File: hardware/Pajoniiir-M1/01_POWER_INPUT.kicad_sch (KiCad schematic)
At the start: 17 parts, among them J1 5V_LOCKING_INPUT_TBD, U7 TPS259474ARPWR

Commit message: hardware: declare verified rail power sources for ERC
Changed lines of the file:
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@@
     (effects (font (size 1.27 1.27)))
+  )
+  (symbol
+    (lib_id "power:PWR_FLAG")
+    (at 120.015 50.165 0)
+    (unit 1)
+    (exclude_from_sim no)
+    (in_bom yes)
+    (on_board yes)
+    (dnp no)
+    (property "Reference" "#FLG0101" (at 120.015 52.07 0) (effects (font (size 1.27 1.27)) (hide yes)))
+    (property "Value" "PWR_FLAG" (at 120.015 53.975 0) (effects (font (size 1.27 1.27))))
+    (property "Footprint" "" (at 120.015 50.165 0) (effects (font (size 1.27 1.27)) (hide yes)))
+    (property "Datasheet" "~" (at 120.015 50.165 0) (effects (font (size 1.27 1.27)) (hide yes)))
+    (property "Description" "Special symbol for telling ERC where power comes from" (at 120.015 50.165 0) (effects (font (size 1.27 1.27)) (hide yes)))
+    (pin "1")
+    (instances (project "Pajoniiir-M1" (path "/2c8dd352-b7b8-4d9e-8f93-5dd43be2a100/31000001-6b2a-4a3a-8c91-000000000001" (reference "#FLG0101") (unit 1))))
+  )
+  (symbol
+    (lib_id "power:PWR_FLAG")
+    (at 19.685 47.625 0)
+    (unit 1)
+    (exclude_from_sim no)
+    (in_bom yes)
+    (on_board yes)
+    (dnp no)
+    (property "Reference" "#FLG0102" (at 19.685 49.53 0) (effects (font (size 1.27 1.27)) (hide yes)))
+    (property "Value" "PWR_FLAG" (at 19.685 51.435 0) (effects (font (size 1.27 1.27))))
+    (property "Footprint" "" (at 19.685 47.625 0) (effects (font (size 1.27 1.27)) (hide yes)))
+    (property "Datasheet" "~" (at 19.685 47.625 0) (effects (font (size 1.27 1.27)) (hide yes)))
+    (property "Description" "Special symbol for telling ERC where power comes from" (at 19.685 47.625 0) (effects (font (size 1.27 1.27)) (hide yes)))
+    (pin "1")
+    (instances (project "Pajoniiir-M1" (path "/2c8dd352-b7b8-4d9e-8f93-5dd43be2a100/31000001-6b2a-4a3a-8c91-000000000001" (reference "#FLG0102") (unit 1))))
   )
   (sheet_instances

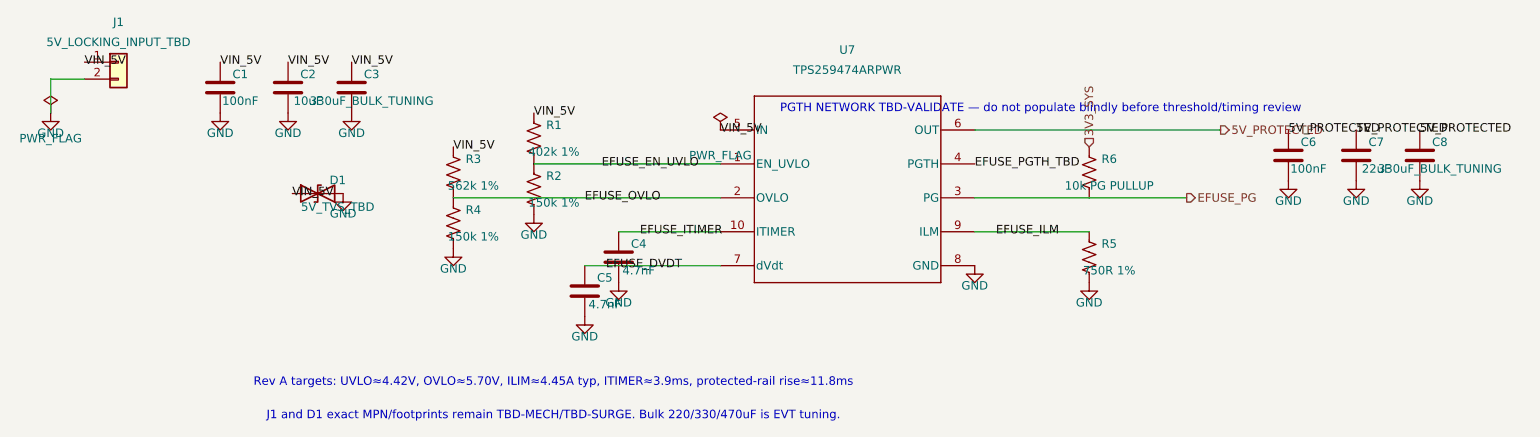
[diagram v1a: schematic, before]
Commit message: hardware: lock TPS259474 PGTH at 4.49V
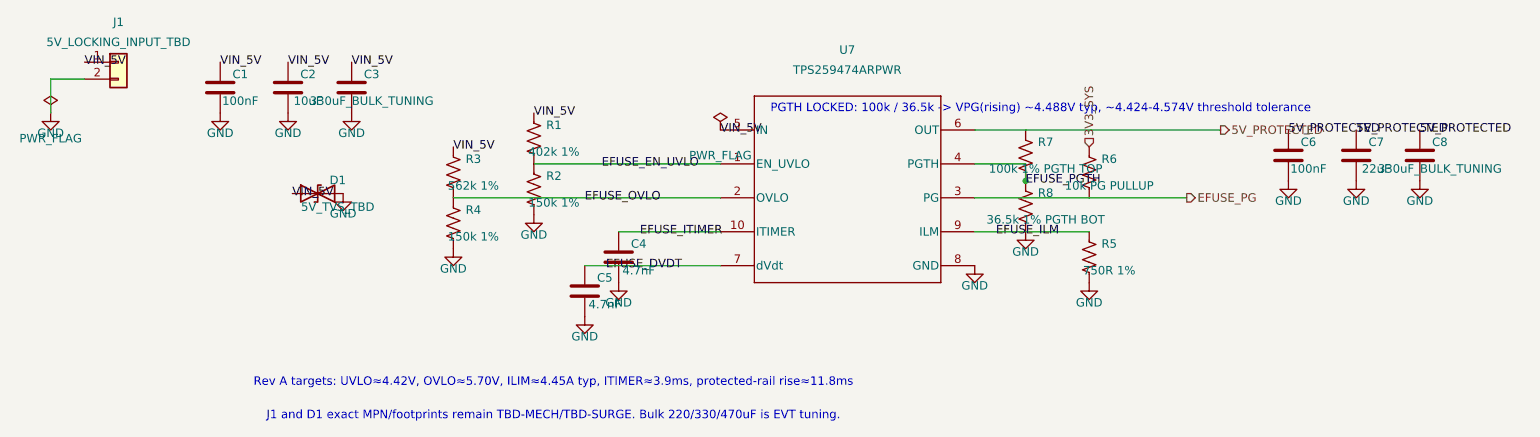
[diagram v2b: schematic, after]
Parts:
- added R7: 100k 1% PGTH TOP, Resistor_SMD:R_0603_1608Metric, symbol Device:R_US
- added R8: 36.5k 1% PGTH BOT, Resistor_SMD:R_0603_1608Metric, symbol Device:R_US
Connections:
- net GND: now also R8.2
- net EFUSE_PGTH_TBD renamed EFUSE_PGTH
- net EFUSE_PGTH: now also R7.2, R8.1
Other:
- note added: "PGTH LOCKED: 100k / 36.5k -> VPG(rising) ~4.488V typ, ~4.424-4.574V threshold tolerance"
- note removed: "PGTH NETWORK TBD-VALIDATE — do not populate blindly before threshold/timing review"
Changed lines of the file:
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@@
     (effects (font (size 1.27 1.27)))
   )
-  (label "EFUSE_PGTH_TBD" (at 158.115 55.245 0)
+  (label "EFUSE_PGTH" (at 165.735 57.785 0)
     (effects (font (size 1.27 1.27)))
   )
-  (text "PGTH NETWORK TBD-VALIDATE — do not populate blindly before threshold/timing review"
+  (wire (pts (xy 158.115 55.245) (xy 165.735 55.245))
+    (stroke (width 0) (type default))
+  )
+  (wire (pts (xy 165.735 55.245) (xy 165.735 57.785))
+    (stroke (width 0) (type default))
+  )
+  (junction (at 165.735 57.785) (diameter 0) (color 0 0 0 0)
+  )
+  (symbol
+    (lib_id "Device:R_US")
+    (at 165.735 53.975 0)
+    (unit 1)
+    (exclude_from_sim no)
+    (in_bom yes)
+    (on_board yes)
+    (dnp no)
+    (property "Reference" "R7" (at 168.735 51.975 0) (effects (font (size 1.27 1.27))))
+    (property "Value" "100k 1% PGTH TOP" (at 168.735 55.975 0) (effects (font (size 1.27 1.27))))
+    (property "Footprint" "Resistor_SMD:R_0603_1608Metric" (at 165.735 53.975 0) (effects (font (size 1.27 1.27)) (hide yes)))
+    (property "Datasheet" "~" (at 165.735 53.975 0) (effects (font (size 1.27 1.27)) (hide yes)))
+    (pin "1")
+    (pin "2")
+    (instances
+      (project "Pajoniiir-M1"
+        (path "/2c8dd352-b7b8-4d9e-8f93-5dd43be2a100/31000001-6b2a-4a3a-8c91-000000000001" (reference "R7") (unit 1))
+      )
+    )
+  )
+  (symbol
+    (lib_id "Device:R_US")
+    (at 165.735 61.595 0)
+    (unit 1)
+    (exclude_from_sim no)
+    (in_bom yes)
+    (on_board yes)
+    (dnp no)
+    (property "Reference" "R8" (at 168.735 59.595 0) (effects (font (size 1.27 1.27))))
+    (property "Value" "36.5k 1% PGTH BOT" (at 168.735 63.595 0) (effects (font (size 1.27 1.27))))
+    (property "Footprint" "Resistor_SMD:R_0603_1608Metric" (at 165.735 61.595 0) (effects (font (size 1.27 1.27)) (hide yes)))
+    (property "Datasheet" "~" (at 165.735 61.595 0) (effects (font (size 1.27 1.27)) (hide yes)))
+    (pin "1")
+    (pin "2")
+    (instances
+      (project "Pajoniiir-M1"
+        (path "/2c8dd352-b7b8-4d9e-8f93-5dd43be2a100/31000001-6b2a-4a3a-8c91-000000000001" (reference "R8") (unit 1))
+      )
+    )
+  )
+  (symbol
+    (lib_id "power:GND")
+    (at 165.735 65.405 0)
+    (unit 1)
+    (exclude_from_sim no)
+    (in_bom yes)
+    (on_board yes)
+    (dnp no)
+    (property "Reference" "#PWR0115" (at 165.735 71.405 0) (effects (font (size 1.27 1.27)) (hide yes)))
+    (property "Value" "GND" (at 165.735 68.405 0) (effects (font (size 1.27 1.27))))
+    (property "Footprint" "" (at 165.735 65.405 0) (effects (font (size 1.27 1.27)) (hide yes)))
+    (property "Datasheet" "" (at 165.735 65.405 0) (effects (font (size 1.27 1.27)) (hide yes)))
+    (pin "1")
+    (instances
+      (project "Pajoniiir-M1"
+        (path "/2c8dd352-b7b8-4d9e-8f93-5dd43be2a100/31000001-6b2a-4a3a-8c91-000000000001" (reference "#PWR0115") (unit 1))
+      )
+    )
+  )
+  (text "PGTH LOCKED: 100k / 36.5k -> VPG(rising) ~4.488V typ, ~4.424-4.574V threshold tolerance"
     (exclude_from_sim no)
     (at 168 47 0)

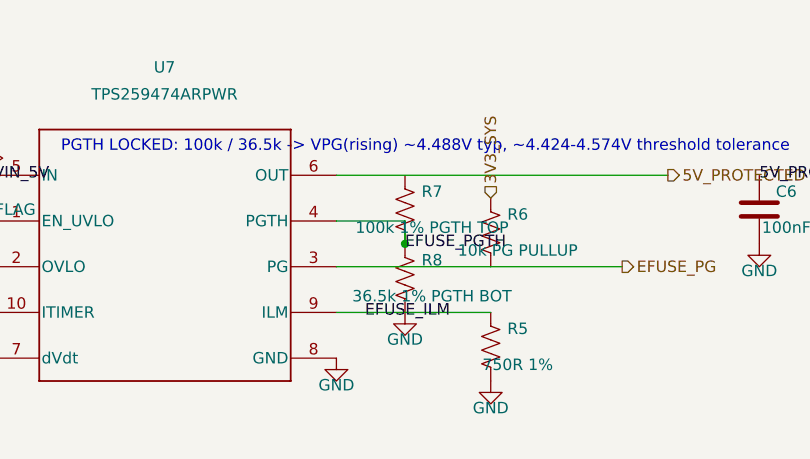
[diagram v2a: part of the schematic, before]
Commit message: ci: capture KiCad 9 symbols and repair PGTH junction
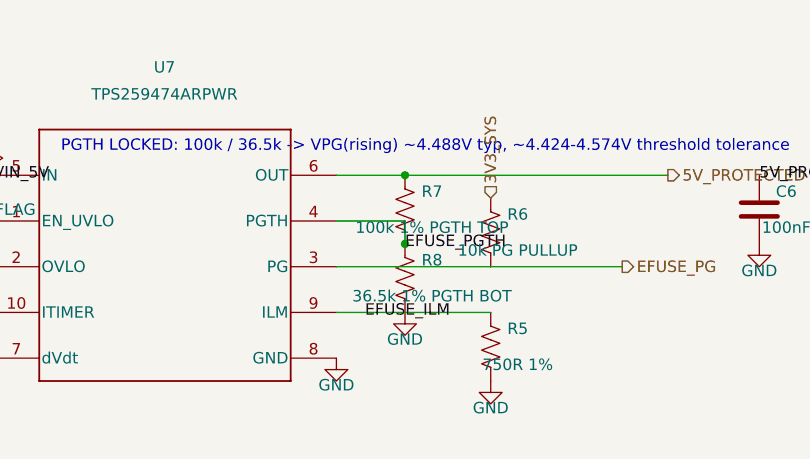
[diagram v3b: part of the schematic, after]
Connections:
- net 5V_PROTECTED: now also R7.1
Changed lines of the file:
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@@
     (stroke (width 0) (type default))
+  )
+  (junction (at 165.735 50.165) (diameter 0) (color 0 0 0 0)
   )
   (hierarchical_label "5V_PROTECTED"
